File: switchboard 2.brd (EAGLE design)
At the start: 100 x 60 mm, 150 parts, among them IC1 4053D, IC10 TC7660-SOIC, IC11 LM317LD, IC12 74HC595D, IC13 74AHC1G125DBV, IC2 4053D, IC3 4053D, IC4 4053D, IC5 FT232RL, IC6 74AHC1G125DBV, IC7 TC7660-SOIC, IC8 SPI_MEMORY-SOIC, IC9 NE5532N, X1 MINI-USB-SCHIELD-32005-301

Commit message: Desenvolvimento do esquematico: adicao de regulador ua78L05, alteracoes nos pinos do MCU, etc.
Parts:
- removed C27: 100n, rcl:C0805
- removed IC13: 74AHC1G125DBV, 74xx-little-de:SOT23-5
- removed R1: (no value), rcl:R0805
- removed R52: 1k SMD, rcl:R0805
- removed R53: 10k SMD, rcl:R0805
- removed R54: 4k7 SMD, rcl:R0805
- removed SJ4, SJ5: (no value), jumper:SJ
- added C12, C15: 100n, rcl:C0603
- added C13: 100n, rcl:C0805
- added D13, D14: LL4148, diode:MINIMELF
- added IC14, IC15: 74LVC1G125DBV, 74xx-little-de:SOT23-5
- added JP7, JP8, JP9: (no value), pinhead:1X02
- D1, D2: value (none) -> LL4148; device diode:SOD80C -> diode:MINIMELF
- D3: value (none) -> LL4148
- IC11: value LM317LD -> LMV321M5; device linear:SO08 -> linear:SOT23-5
- IC6: value 74AHC1G125DBV -> 78L05F; device 74xx-little-de:SOT23-5 -> linear:SOT89
- IC9: value NE5532N -> NE5532D; device linear:DIL08 -> linear:SO08
- R2, R24, R25, R3, R4, R69, R7, R70: device rcl:R0805 -> rcl:R0603
- moved IC11 406.7 mm to (-109.9, -311.8), flipped to the top, turned to 0 degrees
- moved D2 376.2 mm to (-94.6, -298.4), turned to 0 degrees
- moved D1 373.6 mm to (-94.6, -292.1), turned to 0 degrees
- moved D3 372.7 mm to (-94.6, -304.8), flipped to the top, turned to 0 degrees
- moved IC6 252.8 mm to (-102.9, -302.3)
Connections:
- removed net N$1: LED1.C, R1.2
- removed net N$11: C27.1, IC11.4, R52.1, R53.2, R54.2
- removed net N$12: U$1.18
- removed net N$13: R10.2
- removed net N$15: R11.2
- removed net N$17: U$1.15
- removed net N$18: U$1.11
- removed net N$19: R12.2
- removed net N$21: R13.2
- removed net N$27: D1.A, D2.A
- removed net N$7: R9.2
- removed net N$9: R8.2
- new net STAT_LED: LED1.C, U$1.20
- net +3V3: now also C12.1, C15.1, D13.C, IC11.5, IC12.10, IC12.16, IC14.5
- net +5V: now also C13.1, C7.1, D2.C, IC15.5, IC6.1, IC9.8; no longer IC11.2, IC11.3, IC11.6, IC11.7, IC12.10, IC12.16, IC13.5, IC6.5, R52.2
- net -5V: now also C7.2, IC9.4
- net AD0: now also D13.A, D14.C, IC11.1, IC11.3, IC11.4
- net BTN0: now also JP9.1
- net BTN1: now also JP8.1
- net BTN2: now also JP7.1
- net BTN5: now also JP7.2, JP8.2, JP9.2, U$1.7
- net CS_MEM: now also U$1.8; no longer U$1.20
- net C_SW1: now also R9.2, U$1.23
- net C_SW2: now also R8.2, U$1.15
- net C_SW3: now also R10.2, U$1.25
- net C_SW4: now also R11.2, U$1.26
- net C_SW5: now also R12.2, U$1.11
- net C_SW6: now also R13.2, U$1.18
- net GND: now also C12.2, C13.2, C15.2, D1.A, D14.A, IC11.2, IC14.3, IC15.3, IC6.2, IC6.2@1; no longer C27.2, C7.2, D1.C, IC13.3, IC6.3, IC9.4, R1.1, R53.1, R54.1
- net MCU_SW1: no longer U$1.23
- net MCU_SW3: no longer U$1.25
- net MCU_SW4: no longer U$1.26
- net N$100: now also IC14.2; no longer IC6.2
- net N$2: now also IC15.4; no longer IC13.4
- net N$4: now also D1.C, D2.A; no longer D2.C
- net SW3-4: now also SJ3.1; no longer SJ5.1
- net SW4-5: no longer SJ4.1, SJ5.2
- net SW5-6: no longer SJ3.1, SJ4.2
- net UART_RX: now also IC14.4; no longer IC6.4
- net UART_TX: now also IC15.2; no longer IC13.2
- net USB_DETECT: now also IC14.1, IC15.1; no longer IC13.1, IC6.1
- net VCC: now also IC6.3; no longer C7.1, IC11.1, IC9.8
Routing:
- net SW3-4: track 59.0 -> 0.00 mm, vias 2 -> 0
- net +5V: track 46.4 -> 0.62 mm
- net SW4-5: track 21.5 -> 0.00 mm, vias 2 -> 0
- net N$11: track 10.7 -> 0.00 mm
- net MCU_SW4: track 13.7 -> 4.92 mm
- net VCC: track 20.5 -> 12.3 mm
- net MCU_SW3: track 11.3 -> 4.78 mm
- net MCU_SW1: track 10.8 -> 4.76 mm
- net C_SW4: track 0.00 -> 5.18 mm
- net C_SW1: track 1.27 -> 5.17 mm
- net C_SW3: track 1.27 -> 4.65 mm
- net SW5-6: track 3.12 -> 0.00 mm
- net N$27: track 2.29 -> 0.00 mm
- net N$2: track 2.89 -> 0.61 mm
- net N$3: track 13.0 -> 14.5 mm
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
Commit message: Desenvolvimento do esquematico: alteracao para uso de regulador zener para 3.3V, alteracoes no optoacoplador e circuito MIDI, etc.
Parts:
- removed D13, D14: LL4148, diode:MINIMELF
- removed OK1: ILD213, optocoupler:SOIC08
- added C21: 100n, rcl:C0805
- added R1, R38: 100, rcl:R0603
- added R39, R41, R42, R43: 1M SMD, rcl:R0603
- added R44: x, rcl:R0603
- added SJ2: (no value), jumper:SJ
- added U$5: SFH6156 OPTO, PATSKO:DIL4-SMD
- D12: value SS14 -> LL4148; device LUIS:SMA -> diode:MINIMELF
- D7, D8: value LL4148 -> 3V3 ZENER; device diode:MINIMELF -> diode:SOD80C
- R34, R35, R5: value 220 SMD -> 100
- R61: value 1k SMD -> 1k
- R62, R63, R64, R65, R66, R67, R68: value 1k SMD -> 1k; device rcl:R0805 -> rcl:R0603
- R69, R70: value x SMD -> x
- moved D9 505.4 mm to (-130.8, -422.3), flipped to the top, turned to 0 degrees
- moved D8 476.3 mm to (-130.8, -387.4), flipped to the top, turned to 0 degrees
- moved D7 435.5 mm to (-110.5, -352.4), flipped to the top
- moved D12 383.6 mm to (-130.8, -415.9)
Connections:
- removed net N$16: IC12.9, JP18.10
- removed net N$32: D7.C, D8.A
- removed net N$35: D8.C, D9.A
- new net N$1: IC9.2, R39.2, R41.2
- new net N$7: IC9.6, R42.2, R43.2
- new net N$9: C21.1, SJ2.1, X1.M1, X1.M2, X1.M3, X1.M4
- net +3V3: now also C13.1, D12.C, D7.C, IC15.5, R1.1, R35.1, R38.1, R44.2; no longer D13.C, D9.C
- net +5V: now also R1.2, R38.2; no longer C13.1, D7.A, IC15.5, R35.1
- net AD0: now also D12.A, D9.C, R44.1; no longer D13.A, D14.C
- net GND: now also C21.2, D7.A, D8.A, D9.A, R39.1, R43.1, SJ2.2, U$5.3; no longer D14.A, OK1.7
- net MIDI_IN2: now also U$5.2; no longer OK1.2
- net N$100: now also U$5.4; no longer OK1.8
- net N$28: now also U$5.1; no longer OK1.1
- net N$8: now also R42.1; no longer IC9.6
- net SW1_IN: now also R41.1; no longer IC9.2
- net USB_DETECT: now also D8.C
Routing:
- net N$8: track 6.33 -> 0.00 mm
- net +3V3: track 24.9 -> 19.1 mm
- net N$28: track 15.5 -> 10.2 mm
- net MIDI_IN2: track 6.92 -> 3.38 mm
- net N$35: track 2.92 -> 0.00 mm
- net N$32: track 2.92 -> 0.00 mm
- net SW1_IN: track 31.3 -> 30.1 mm
- net +5V: track 0.62 -> 0.00 mm

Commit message: Switch arrangement changed from 4053 to crosspoint switch.
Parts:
- removed C28: (no value), rcl:E2,5-6
- removed C31, C35: 1u 0805, rcl:C0805
- removed C32, C34, C36: 1u SMC, rcl:SMC_B
- removed C37, C38, C39, C40, C41: x, rcl:C0603
- removed IC10, IC7: TC7660-SOIC, LUIS:SO08
- removed LED1: (no value), led:CHIPLED_0805
- removed R30, R31, R32, R33, R36, R37, R40: 1M, rcl:R0805
- added C22, C23, C27: 100n, rcl:C0805
- added D13, D14: LL4148, diode:MINIMELF
- added L1: FERRITE_BEAD, PATSKO:0805
- added P_INPUT2, P_OUT1: (no value), pinhead:1X02
- C10, C11: value x -> (none); device rcl:C0603 -> rcl:E2,5-6
- C14, C3: value x -> 100n
- C16: value (none) -> 47u/25V; device rcl:SMC_C -> PATSKO:ALUMINUM-TANTALUM-CAP
- C17: value (none) -> 47u/25V; device rcl:UD-6,3X5,8_NICHICON -> PATSKO:ALUMINUM-TANTALUM-CAP
- C18: value x -> 100n; device rcl:C0603 -> rcl:C0805
- C19, C20: value x -> 1u; device rcl:C0603 -> PATSKO:SMB-SMA-0805-0603
- C25: value (none) -> 100n; device rcl:SMC_C -> rcl:C0805
- C5, C8: value 1u 0805 -> 1u; device rcl:C0805 -> PATSKO:SMB-SMA-0805-0603
- C9: value 1u SMC -> 47u/25V; device rcl:SMC_B -> PATSKO:ALUMINUM-TANTALUM-CAP
- IC1: value 4053D -> MT8816AP; device 40xx:SO16 -> PATSKO:PLCC44
- IC17: value SFH6156 OPTO -> PC817S OPTO
- IC2: value 4053D -> NE5532D; device 40xx:SO16 -> linear:SO08
- IC3, IC4: value 4053D -> TC7660-SOIC; device 40xx:SO16 -> PATSKO:SOIC08
- IC8: device PATSKO:SO08 -> PATSKO:SOIC08
- R14, R27: device rcl:R0805 -> rcl:R0603
- R15: value 1M -> 10k
- R16, R18, R19, R26, R28, R29: value 1M -> 1M SMD; device rcl:R0805 -> rcl:R0603
- R17, R23: value 1M -> 1k SMD; device rcl:R0805 -> rcl:R0603
- R22: value 10k -> 1k
- SJ3: device jumper:SJ -> jumper:SJ_2
- moved C8 600.1 mm to (-193.7, -488.9), flipped to the top, turned to 0 degrees
- moved SJ3 582.4 mm to (-217.8, -495.3), turned to 0 degrees
- moved C25 536.9 mm to (-219.1, -512.4)
- moved C17 526.2 mm to (-217.2, -486.4)
- moved C16 522.7 mm to (-208.9, -486.4)
- moved IC2 498.5 mm to (-148.0, -448.3), turned to 0 degrees
- moved IC1 479.3 mm to (-143.5, -415.3), turned to 0 degrees
- moved C5 396.9 mm to (-163.2, -488.9)
- moved C3 351.8 mm to (-151.1, -428.0)
- moved R14 346.5 mm to (-142.9, -461.0)
- moved C14 285.3 mm to (-135.9, -476.9)
- moved C10 283.8 mm to (-140.3, -445.1)
- moved C11 276.7 mm to (-130.8, -445.1)
- moved R17 271.6 mm to (-151.1, -476.9)
- moved IC4 268.4 mm to (-179.1, -487.7)
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- renumbered MICRO_XP to IC19, U$1 to IC18, U$2 to IC16, U$5 to IC17
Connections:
- net INPUT renamed INPUT1
- net OUTPUT renamed OUTPUT1
- removed net E_IN7: C41.1, IC4.15, R29.2
- removed net STAT_LED: IC18.20, LED1.C
- removed net SW1-2: IC1.15, IC1.5, IC2.13, R23.2
- removed net SW1_IN: IC1.1, IC1.12, IC9.1, R41.1, R7.2
- removed net SW2-3: IC2.14, IC2.2, IC2.3, R30.2
- removed net SW3-4: IC2.4, IC3.1, IC3.12, R16.2, SJ3.1
- removed net SW4-5: IC3.15, IC3.5, IC4.13, R37.2
- removed net SW5-6: IC4.14, IC4.2, IC4.3, R28.2
- removed net SW_EFF_IN1: C37.1, IC1.14, R19.2
- removed net SW_EFF_IN2: C38.1, IC1.4, R26.2
- removed net SW_EFF_IN3: C19.1, IC3.14, R36.2
- removed net SW_EFF_IN4: C20.1, IC3.4, R40.2
- removed net SW_EFF_OUT1: C3.2, IC1.2, R14.2
- removed net SW_EFF_OUT2: C18.2, IC3.2, R27.2
- new net CS_SWITCH: IC1.40, IC18.21
- new net C_SW7: IC1.2, IC18.20
- new net INPUT2: P_INPUT2.2, R17.2
- new net N$11: C3.1, IC1.3, R15.1
- new net N$12: IC1.39
- new net N$13: IC1.41
- new net N$15: IC1.43
- new net N$16: IC1.1
- new net N$17: IC1.23
- new net N$18: IC1.21
- new net N$19: IC1.19
- new net N$21: IC1.17
- new net N$27: C10.+, IC2.3, R16.2
- new net N$32: IC1.36
- new net N$35: IC1.35
- new net N$52: IC1.10
- new net N$53: IC1.11
- new net N$54: C10.-, D13.C, D14.A, R14.2, R17.1
- new net N$55: C11.+, IC2.7, R28.1
- new net N$56: C11.-, R19.2, R23.2
- new net N$57: IC2.2, R26.2, R27.2
- new net N$58: IC2.6, R28.2, R29.2
- new net N$59: L1.1, X1.1
- new net N$60: C20.-, IC4.2
- new net OUTPUT2: P_OUT1.1, R23.1
- new net SW_IN_1: IC1.37, IC2.1, IC9.1, R18.2, R27.1, R41.1, R7.2
- net +18V: now also C8.+; no longer C8.2, C9.+
- net +3V3: now also C18.1, C27.1; no longer LED1.A
- net +5V: now also C14.1, C17.+, C23.1, C25.1, D14.C, IC1.44, IC2.8, IC3.8, R15.2; no longer C28.+, IC1.16, IC10.8, IC2.16, IC3.16, IC4.16
- net -5V: now also C14.2, C19.-, IC1.22, IC2.4, IC3.5; no longer C35.2, C36.+, IC1.7, IC10.5, IC2.7, IC3.7, IC4.7
- net C_SW1: now also IC1.5; no longer IC1.10, IC1.11
- net C_SW2: now also IC1.24; no longer IC1.9, IC2.11
- net C_SW3: now also IC1.25; no longer IC2.10, IC2.9
- net C_SW4: now also IC1.4; no longer IC3.10, IC3.11
- net C_SW5: now also IC1.26; no longer IC3.9, IC4.11
- net C_SW6: now also IC1.27; no longer IC4.10, IC4.9
- net E_IN1: no longer C37.2
- net E_IN2: no longer C38.2
- net E_IN3: no longer C14.1, C14.2, IC2.15, R15.2
- net E_IN4: no longer C19.2
- net E_IN5: no longer C20.2
- net E_IN6: no longer C41.2
- net E_OUT1: no longer C3.1
- net E_OUT2: no longer C10.1
- net E_OUT3: no longer C11.1
- net E_OUT4: no longer C18.1
- net E_OUT5: no longer C39.1
- net E_OUT6: no longer C40.1
- net GND: now also C18.2, C19.+, C22.2, C23.2, C25.2, C27.2, C3.2, C8.-, D13.A, IC1.18, IC4.3, IC4.5, P_INPUT2.1, P_OUT1.2; no longer C25.-, C28.-, C35.1, C36.-, C8.1, IC1.13, IC1.3, IC1.6, IC1.8, IC10.3, IC2.1, IC2.6, IC2.8, IC3.13, IC3.6, IC3.8, IC4.1, IC4.6, IC4.8, IC7.3, IC7.5, R15.1, R17.1, R23.1, R27.1, R28.1, R30.1, R31.1, R32.1, R33.1, R36.1, R37.1, R40.1
- net MOSI: now also IC1.42
- net N$10: now also C20.+; no longer C31.1, C32.+
- net N$2: now also SJ3.3
- net N$25: now also C16.+; no longer C25.+
- net N$44: now also IC14.4, SJ3.2; no longer IC10.1, SJ1.1
- net N$46: now also C5.+, IC3.2; no longer C34.-, C5.2, IC10.2
- net N$47: now also C5.-, IC3.4; no longer C34.+, C5.1, IC10.4
- net N$48: now also IC1.34; no longer C10.2, IC2.12, R17.2
- net N$49: now also IC1.33; no longer C11.2, IC2.5, R18.2
- net N$5: now also IC3.1, SJ1.1; no longer IC7.1, SJ6.1
- net N$50: now also IC1.32; no longer C39.2, IC4.12, R32.2
- net N$51: now also IC1.9; no longer C40.2, IC4.5, R33.2
- net N$6: now also IC4.1, SJ6.1; no longer C31.2, C32.-, IC7.2
- net SCK: now also IC1.20
- net SW6: now also IC2.5; no longer IC4.4, R31.2, SJ3.2
- net UART_RX: now also SJ3.1; no longer IC14.4
- net VCC: now also C22.1, C9.+, IC4.8; no longer C16.+, C17.+, IC7.8
- net VCCUSB: now also L1.2; no longer X1.1
- net XP_RST: no longer IC18.21
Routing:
- net SW1_IN: track 30.1 -> 0.00 mm, vias 2 -> 0
- net SW1-2: track 25.6 -> 0.00 mm, vias 2 -> 0
- net SW_IN_1: track 0.00 -> 23.0 mm, vias 0 -> 2
- net C_SW2: track 16.3 -> 0.00 mm, vias 2 -> 0
- net +18V: track 12.3 -> 0.00 mm, vias 1 -> 0
- net N$6: track 10.6 -> 0.00 mm
- net N$5: track 4.90 -> 0.00 mm
- net SW6: track 45.1 -> 42.7 mm
- net XP_RST: track 6.61 -> 4.50 mm
- net N$10: track 8.40 -> 6.52 mm
- net SW2-3: track 1.27 -> 0.00 mm
- net C_SW3: track 4.65 -> 3.38 mm
- net C_SW1: track 5.17 -> 3.90 mm

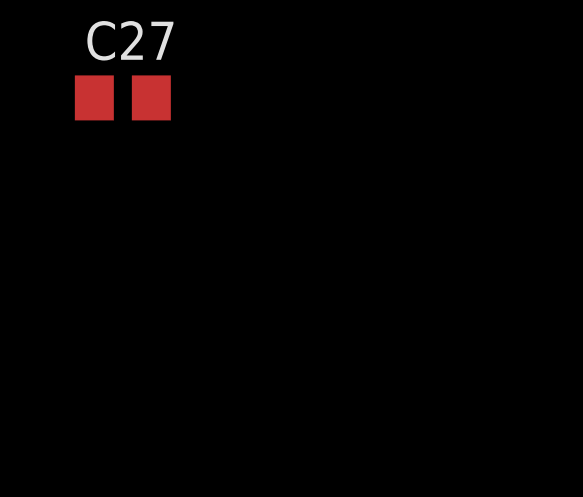
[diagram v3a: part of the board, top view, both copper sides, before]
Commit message: Addition of MIDI Thru mounting option. Routing of crosspoint switch input and output signals.
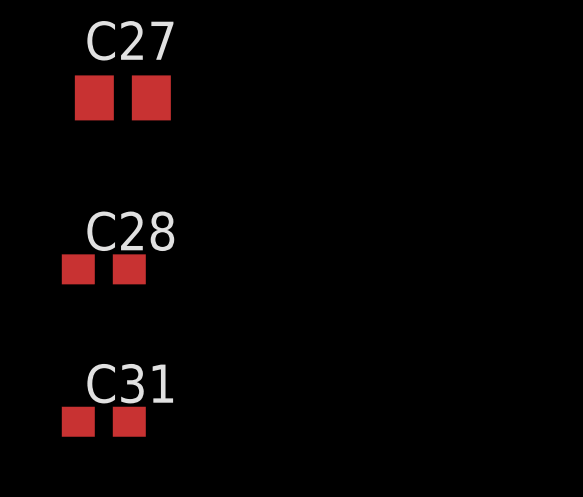
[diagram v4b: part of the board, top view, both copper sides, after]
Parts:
- added C28, C31: 100n, rcl:C0603
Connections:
- net N$52 renamed EIN_7
- net N$53 renamed EIN_8
- removed net E_IN1: JP17.1
- removed net E_IN2: JP17.3
- removed net E_IN3: JP17.5
- removed net E_IN4: JP24.1
- removed net E_IN5: JP24.3
- removed net E_IN6: JP24.5
- removed net E_OUT1: JP10.1
- removed net E_OUT2: JP10.3
- removed net E_OUT3: JP10.5
- removed net E_OUT4: JP11.1
- removed net E_OUT5: JP11.3
- removed net E_OUT6: JP11.5
- removed net N$12: IC1.39
- removed net N$13: IC1.41
- removed net N$15: IC1.43
- removed net N$16: IC1.1
- removed net N$17: IC1.23
- removed net N$18: IC1.21
- removed net N$19: IC1.19
- removed net N$21: IC1.17
- removed net N$32: IC1.36
- removed net SW6: IC2.5, IC9.5
- new net EIN_2: IC1.35, JP17.3
- new net EIN_3: IC1.34, JP17.5
- new net EIN_4: IC1.33, JP24.1
- new net EIN_5: IC1.32, JP24.3
- new net EIN_6: IC1.9, JP24.5
- new net EIN_9: IC1.12
- new net EOUT_1: IC1.41, JP10.1
- new net EOUT_2: IC1.43, JP10.3
- new net EOUT_3: IC1.1, JP10.5
- new net EOUT_4: IC1.23, JP11.1
- new net EOUT_5: IC1.21, JP11.3
- new net EOUT_6: IC1.19, JP11.5
- new net N$61: IC15.2, SJ3.2
- new net SWIN_2-EIN_1: IC1.36, IC2.1, JP17.1, R18.2, R27.1
- new net SWOUT_1: IC1.39, IC9.5
- new net SWOUT_2-EOUT_7: IC1.17, IC2.5
- net +5V: now also C28.1
- net -5V: now also C31.2
- net GND: now also C28.2, C31.1, IC1.8
- net N$2: no longer SJ3.3
- net N$35: now also IC1.7; no longer IC1.35
- net N$44: now also IC12.9, JP18.10; no longer IC14.4, SJ3.2
- net N$48: now also IC1.30; no longer IC1.34
- net N$49: now also IC1.31; no longer IC1.33
- net N$50: now also IC1.14; no longer IC1.32
- net N$51: now also IC1.13; no longer IC1.9
- net SW_IN_1: no longer IC2.1, R18.2, R27.1
- net UART_RX: now also IC14.4
- net UART_TX: now also SJ3.3; no longer IC15.2
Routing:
- net SWOUT_1: track 0.00 -> 42.7 mm, vias 0 -> 2
- net SW6: track 42.7 -> 0.00 mm, vias 2 -> 0
- net E_OUT1: track 35.9 -> 0.00 mm, vias 2 -> 0
- net EOUT_1: track 0.00 -> 35.9 mm, vias 0 -> 2
- net E_OUT4: track 35.2 -> 0.00 mm, vias 2 -> 0
- net EOUT_4: track 0.00 -> 35.2 mm, vias 0 -> 2
- net E_OUT6: track 30.4 -> 0.00 mm
- net EOUT_6: track 0.00 -> 30.4 mm
- net E_OUT3: track 27.0 -> 0.00 mm
- net EOUT_3: track 0.00 -> 27.0 mm
- net E_IN5: track 26.9 -> 0.00 mm
- net EIN_5: track 0.00 -> 26.9 mm
- net E_IN2: track 23.8 -> 0.00 mm
- net EIN_2: track 0.00 -> 23.8 mm
- net E_OUT5: track 12.2 -> 0.00 mm
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
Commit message: Ajustes na alimentacao: troca de regulador zener por CJ1117, adicao de diodos OR para 5V, adicao de jumper de selecao para 3.3V, adicao de filtro para 5V analogico. Adicao de pinos para acesso aos sinais de USB.
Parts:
- removed D7: 3V3 ZENER, diode:SOD80C
- removed JP10, JP17, JP24: (no value), pinhead:2X03
- removed R1, R38: 100, rcl:R0603
- added C32: 47u/25V, PATSKO:ALUMINUM-TANTALUM-CAP
- added C34: 100n, rcl:C0805
- added IC7: LD117AS33TR, v-reg:SOT223
- added L2: FERRITE_BEAD, PATSKO:0805
- added SJ4: (no value), jumper:SJ_2
- JP11: device pinhead:2X03 -> pinhead:1X05
- moved JP11 656.3 mm to (-230.5, -558.8), turned to 0 degrees
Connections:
- net VCCUSB renamed 5V_USB
- removed net N$59: L1.1, X1.1
- removed net N$9: C21.1, SJ2.1, X1.M1, X1.M2, X1.M3, X1.M4
- removed net VCC_FT232: C29.1, D10.C, D11.C, IC5.20
- new net 3V3_FTDI: C33.1, IC5.17, SJ4.3
- new net 3V3_REG: C32.+, IC7.4, SJ4.1
- new net N$13: C23.1, D10.A, IC6.1
- new net USB_SHLD: C21.1, JP11.1, SJ2.1, X1.M1, X1.M2, X1.M3, X1.M4
- new net V+: C14.1, C25.1, C28.1, C34.1, C7.1, D14.C, D2.C, IC2.8, IC3.8, IC9.8, L2.2, R15.2, SJ1.2
- new net VIN_USB: JP11.5, L1.1, X1.1
- net +3V3: now also SJ4.2; no longer C27.1, C33.1, D7.C, IC5.17, R1.1, R38.1
- net +5V: now also C29.1, D10.C, D11.C, IC5.20, L2.1; no longer C14.1, C23.1, C25.1, C28.1, C7.1, D10.A, D14.C, D2.C, IC2.8, IC3.8, IC6.1, IC9.8, R1.2, R15.2, R38.2, SJ1.2
- net D+: now also JP11.3
- net D-: now also JP11.4
- net EIN_2: no longer JP17.3
- net EIN_3: no longer JP17.5
- net EIN_4: no longer JP24.1
- net EIN_5: no longer JP24.3
- net EIN_6: no longer JP24.5
- net EOUT_1: no longer JP10.1
- net EOUT_2: no longer JP10.3
- net EOUT_3: no longer JP10.5
- net EOUT_4: no longer JP11.1
- net EOUT_5: no longer JP11.3
- net EOUT_6: no longer JP11.5
- net GND: now also C32.-, C34.2, IC7.1; no longer D7.A, JP10.2, JP10.4, JP10.6, JP11.4, JP11.6, JP17.2, JP17.4, JP17.6, JP24.2, JP24.4, JP24.6
- net SWIN_2-EIN_1: no longer JP17.1
- net VCC: now also C27.1, IC7.3
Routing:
- net EOUT_1: track 35.9 -> 0.00 mm, vias 2 -> 0
- net EOUT_4: track 35.2 -> 0.00 mm, vias 2 -> 0
- net EOUT_6: track 30.4 -> 0.00 mm
- net EOUT_3: track 27.0 -> 0.00 mm
- net EIN_5: track 26.9 -> 0.00 mm
- net EIN_2: track 23.8 -> 0.00 mm
- net EOUT_5: track 12.2 -> 0.00 mm
- net EIN_6: track 5.87 -> 0.00 mm
- net EOUT_2: track 5.72 -> 0.00 mm
- net SWIN_2-EIN_1: track 5.39 -> 0.00 mm
- net EIN_3: track 4.97 -> 0.00 mm
- net EIN_4: track 0.90 -> 0.00 mm

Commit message: Input/output pinheaders and components added. Initial layout adjustments.
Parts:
- added C35, C36, C37, C38, C39, C40, C41, C42, C43, C44, C45, C46, C47, C48, C49, C50, C51, C52: 1u, rcl:C0603
- added JP10, JP15, JP16, JP17, JP19, JP20: (no value), pinhead:2X03
- added R1, R30, R31, R32, R33, R36, R37, R38, R40, R45, R46, R47, R48, R49, R50, R51, R52, R53: 1M, rcl:R0603
- moved JP11 647.1 mm to (1.91, 45.1), turned to 90 degrees
- moved IC7 646.3 mm to (64.8, 49.5), flipped to the bottom
- moved IC3 582.2 mm to (94.0, 31.1), flipped to the bottom, turned to 90 degrees
- moved IC4 578.4 mm to (94.0, 22.2), flipped to the bottom, turned to 90 degrees
- moved IC2 520.6 mm to (81.3, 19.1)
- moved IC1 474.9 mm to (62.2, 12.7)
- moved IC17 429.2 mm to (21.0, 44.5), flipped to the bottom
- moved D1 376.5 mm to (23.5, 65.4), turned to 90 degrees
- moved IC14 344.7 mm to (29.2, 46.4), flipped to the bottom
- moved IC15 340.4 mm to (29.8, 38.7), flipped to the bottom
- moved IC8 143.9 mm to (36.8, 18.4), flipped to the bottom
- moved IC16 95.8 mm to (81.3, 43.2), turned to 90 degrees
- moved IC5 69.0 mm to (8.26, 43.8), flipped to the bottom, turned to 270 degrees
- moved X1 55.7 mm to (4.45, 29.2), flipped to the bottom, turned to 180 degrees
- moved JP1 17.5 mm to (25.7, 31.5)
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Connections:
- net SWIN_2-EIN_1 renamed SWIN_2
- removed net N$35: IC1.7
- removed net N$48: IC1.30
- removed net N$49: IC1.31
- removed net N$50: IC1.14
- removed net N$51: IC1.13
- new net EIN_1: C35.1, IC1.35, R1.1
- new net EIN_10: C50.1, IC1.14, R51.1
- new net EIN_11: C51.1, IC1.31, R52.1
- new net N$12: C35.2, JP10.6
- new net N$15: C36.2, JP10.4
- new net N$16: C37.2, JP10.2
- new net N$17: C38.2, JP15.6
- new net N$18: C39.2, JP15.4
- new net N$19: C40.2, JP15.2
- new net N$21: C41.2, JP16.6
- new net N$32: C42.2, JP16.4
- new net N$52: C43.2, JP16.2
- new net N$53: C44.2, JP17.6
- new net N$59: C45.2, JP17.4
- new net N$62: C46.2, JP17.2
- new net N$63: C48.2, JP19.4
- new net N$64: C49.2, JP19.2
- new net N$65: C50.2, JP20.6
- new net N$66: C51.2, JP20.4
- new net N$67: C52.2, JP20.2
- new net N$9: C47.2, JP19.6
- net +5V: no longer IC1.44
- net EIN_2: now also C36.1, R30.1; no longer IC1.35
- net EIN_3: now also C37.1, R31.1; no longer IC1.34
- net EIN_4: now also C38.1, R36.1; no longer IC1.33
- net EIN_5: now also C39.1, R37.1; no longer IC1.32
- net EIN_6: now also C40.1, R38.1; no longer IC1.9
- net EIN_7: now also C47.1, R32.1; no longer IC1.10
- net EIN_8: now also C48.1, R33.1; no longer IC1.11
- net EIN_9: now also C49.1, IC1.13, R50.1; no longer IC1.12
- net EOUT_1: now also C41.1, R40.1
- net EOUT_2: now also C42.1, R45.1
- net EOUT_3: now also C43.1, R46.1
- net EOUT_4: now also C44.1, R47.1
- net EOUT_5: now also C45.1, R48.1
- net EOUT_6: now also C46.1, R49.1
- net GND: now also IC1.30, IC1.7, JP10.1, JP10.3, JP10.5, JP15.1, JP15.3, JP15.5, JP16.1, JP16.3, JP16.5, JP17.1, JP17.3, JP17.5, JP19.1, JP19.3, JP19.5, JP20.1, JP20.3, JP20.5, R1.2, R30.2, R31.2, R32.2, R33.2, R36.2, R37.2, R38.2, R40.2, R45.2, R46.2, R47.2, R48.2, R49.2, R50.2, R51.2, R52.2, R53.2
- net SWOUT_2-EOUT_7: now also C52.1, R53.1
- net V+: now also IC1.44
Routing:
- net +3V3: track 19.1 -> 28.0 mm
